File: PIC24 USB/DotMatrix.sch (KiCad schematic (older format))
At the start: 13 parts, among them Q2 MOSFET_N, Q3 MOSFET_N, Q4 MOSFET_N, Q5 MOSFET_N, Q6 MOSFET_N, Q7 MOSFET_N, Q8 MOSFET_N, U3 50mm_5x7_Dot_Matrix_Led_Displ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

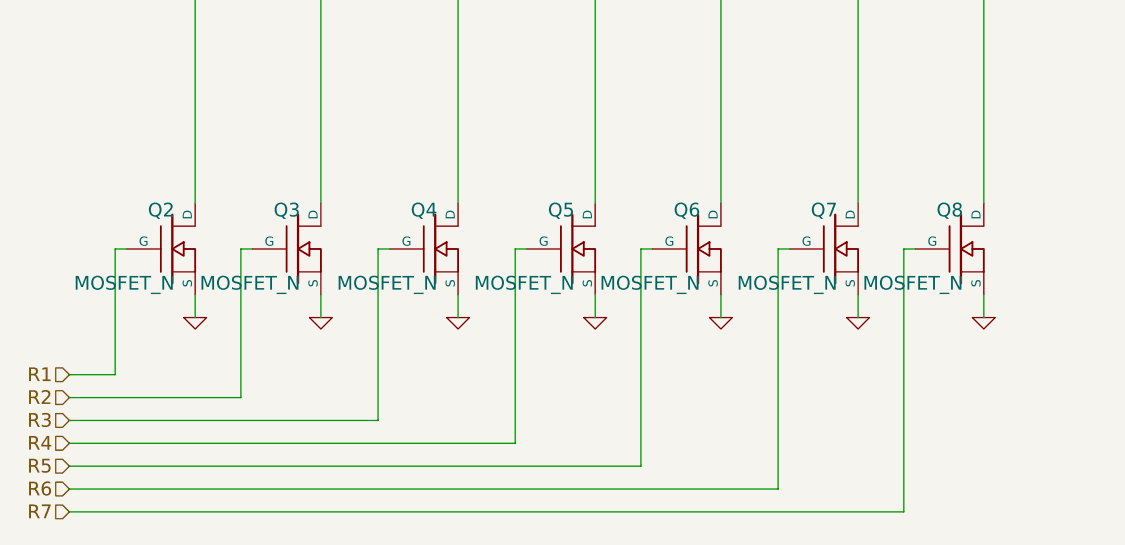
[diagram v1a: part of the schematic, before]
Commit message: shrinked, added temp sensor, updated gerbers and submitted them
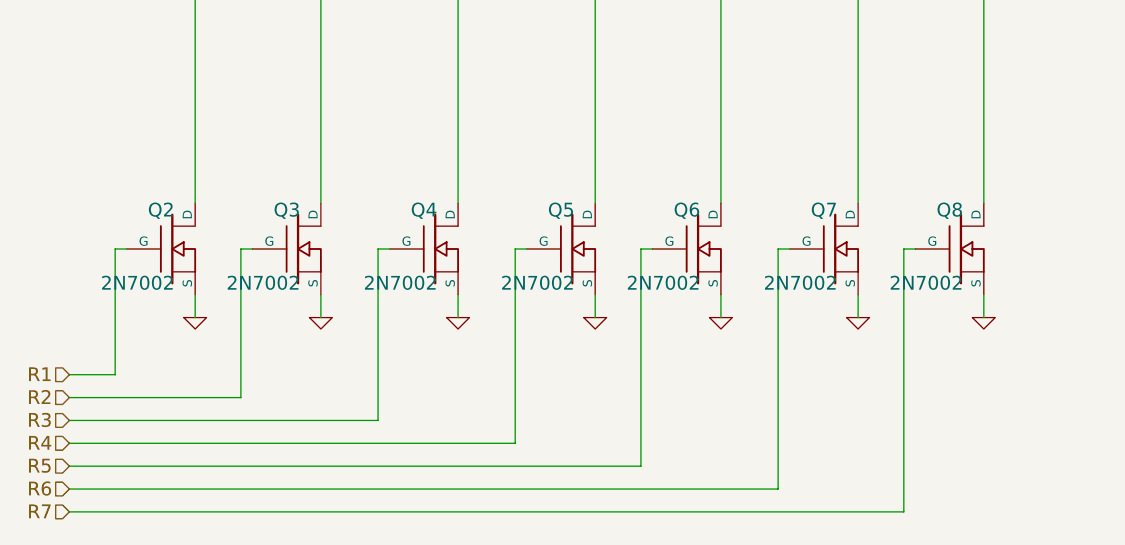
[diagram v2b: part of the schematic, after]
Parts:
- Q2, Q3, Q4, Q5, Q6, Q7, Q8: value MOSFET_N -> 2N7002
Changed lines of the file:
@@
 $Descr A4 11693 8268
 encoding utf-8
-Sheet 3 3
+Sheet 2 3
 Title ""
 Date ""
@@
 P 1200 4700
 F 0 "Q2" H 1210 4870 60  0000 R CNN
-F 1 "MOSFET_N" H 1210 4550 60  0000 R CNN
+F 1 "2N7002" H 1210 4550 60  0000 R CNN
 F 2 "SMD_Packages:SOT-23-GDS" H 1200 4700 60  0001 C CNN
 F 3 "" H 1200 4700 60  0000 C CNN
@@
 P 2350 4700
 F 0 "Q4" H 2360 4870 60  0000 R CNN
-F 1 "MOSFET_N" H 2360 4550 60  0000 R CNN
+F 1 "2N7002" H 2360 4550 60  0000 R CNN
 F 2 "SMD_Packages:SOT-23-GDS" H 2350 4700 60  0001 C CNN
 F 3 "" H 2350 4700 60  0000 C CNN
@@
 P 1750 4700
 F 0 "Q3" H 1760 4870 60  0000 R CNN
-F 1 "MOSFET_N" H 1760 4550 60  0000 R CNN
+F 1 "2N7002" H 1760 4550 60  0000 R CNN
 F 2 "SMD_Packages:SOT-23-GDS" H 1750 4700 60  0001 C CNN
 F 3 "" H 1750 4700 60  0000 C CNN
@@
 P 2950 4700
 F 0 "Q5" H 2960 4870 60  0000 R CNN
-F 1 "MOSFET_N" H 2960 4550 60  0000 R CNN
+F 1 "2N7002" H 2960 4550 60  0000 R CNN
 F 2 "SMD_Packages:SOT-23-GDS" H 2950 4700 60  0001 C CNN
 F 3 "" H 2950 4700 60  0000 C CNN
@@
 P 4100 4700
 F 0 "Q7" H 4110 4870 60  0000 R CNN
-F 1 "MOSFET_N" H 4110 4550 60  0000 R CNN
+F 1 "2N7002" H 4110 4550 60  0000 R CNN
 F 2 "SMD_Packages:SOT-23-GDS" H 4100 4700 60  0001 C CNN
 F 3 "" H 4100 4700 60  0000 C CNN
@@
 P 3500 4700
 F 0 "Q6" H 3510 4870 60  0000 R CNN
-F 1 "MOSFET_N" H 3510 4550 60  0000 R CNN
+F 1 "2N7002" H 3510 4550 60  0000 R CNN
 F 2 "SMD_Packages:SOT-23-GDS" H 3500 4700 60  0001 C CNN
 F 3 "" H 3500 4700 60  0000 C CNN
@@
 P 4650 4700
 F 0 "Q8" H 4660 4870 60  0000 R CNN
-F 1 "MOSFET_N" H 4660 4550 60  0000 R CNN
+F 1 "2N7002" H 4660 4550 60  0000 R CNN
 F 2 "SMD_Packages:SOT-23-GDS" H 4650 4700 60  0001 C CNN
 F 3 "" H 4650 4700 60  0000 C CNN
@@
 	1300 2900 1300 4500
 $Comp
-L GND #PWR35
+L GND #PWR37
 U 1 1 53E9FEF4
 P 1300 5000
-F 0 "#PWR35" H 1300 5000 30  0001 C CNN
+F 0 "#PWR37" H 1300 5000 30  0001 C CNN
 F 1 "GND" H 1300 4930 30  0001 C CNN
 F 2 "" H 1300 5000 60  0000 C CNN
@@
 $EndComp
 $Comp
-L GND #PWR36
+L GND #PWR38
 U 1 1 53E9FF16
 P 1850 5000
-F 0 "#PWR36" H 1850 5000 30  0001 C CNN
+F 0 "#PWR38" H 1850 5000 30  0001 C CNN
 F 1 "GND" H 1850 4930 30  0001 C CNN
 F 2 "" H 1850 5000 60  0000 C CNN
@@
 $EndComp
 $Comp
-L GND #PWR37
+L GND #PWR39
 U 1 1 53E9FF29
 P 2450 5000
-F 0 "#PWR37" H 2450 5000 30  0001 C CNN
+F 0 "#PWR39" H 2450 5000 30  0001 C CNN
 F 1 "GND" H 2450 4930 30  0001 C CNN
 F 2 "" H 2450 5000 60  0000 C CNN
@@
 $EndComp
 $Comp
-L GND #PWR38
+L GND #PWR40
 U 1 1 53E9FF3C
 P 3050 5000
-F 0 "#PWR38" H 3050 5000 30  0001 C CNN
+F 0 "#PWR40" H 3050 5000 30  0001 C CNN
 F 1 "GND" H 3050 4930 30  0001 C CNN
 F 2 "" H 3050 5000 60  0000 C CNN
@@
 $EndComp
 $Comp
-L GND #PWR39
+L GND #PWR41
 U 1 1 53EA0257
 P 3600 5000
-F 0 "#PWR39" H 3600 5000 30  0001 C CNN
+F 0 "#PWR41" H 3600 5000 30  0001 C CNN
 F 1 "GND" H 3600 4930 30  0001 C CNN
 F 2 "" H 3600 5000 60  0000 C CNN
@@
 $EndComp
 $Comp
-L GND #PWR40
+L GND #PWR42
 U 1 1 53EA025D
 P 4200 5000
-F 0 "#PWR40" H 4200 5000 30  0001 C CNN
+F 0 "#PWR42" H 4200 5000 30  0001 C CNN
 F 1 "GND" H 4200 4930 30  0001 C CNN
 F 2 "" H 4200 5000 60  0000 C CNN
@@
 $EndComp
 $Comp
-L GND #PWR41
+L GND #PWR43
 U 1 1 53EA0263
 P 4750 5000
-F 0 "#PWR41" H 4750 5000 30  0001 C CNN
+F 0 "#PWR43" H 4750 5000 30  0001 C CNN
 F 1 "GND" H 4750 4930 30  0001 C CNN
 F 2 "" H 4750 5000 60  0000 C CNN

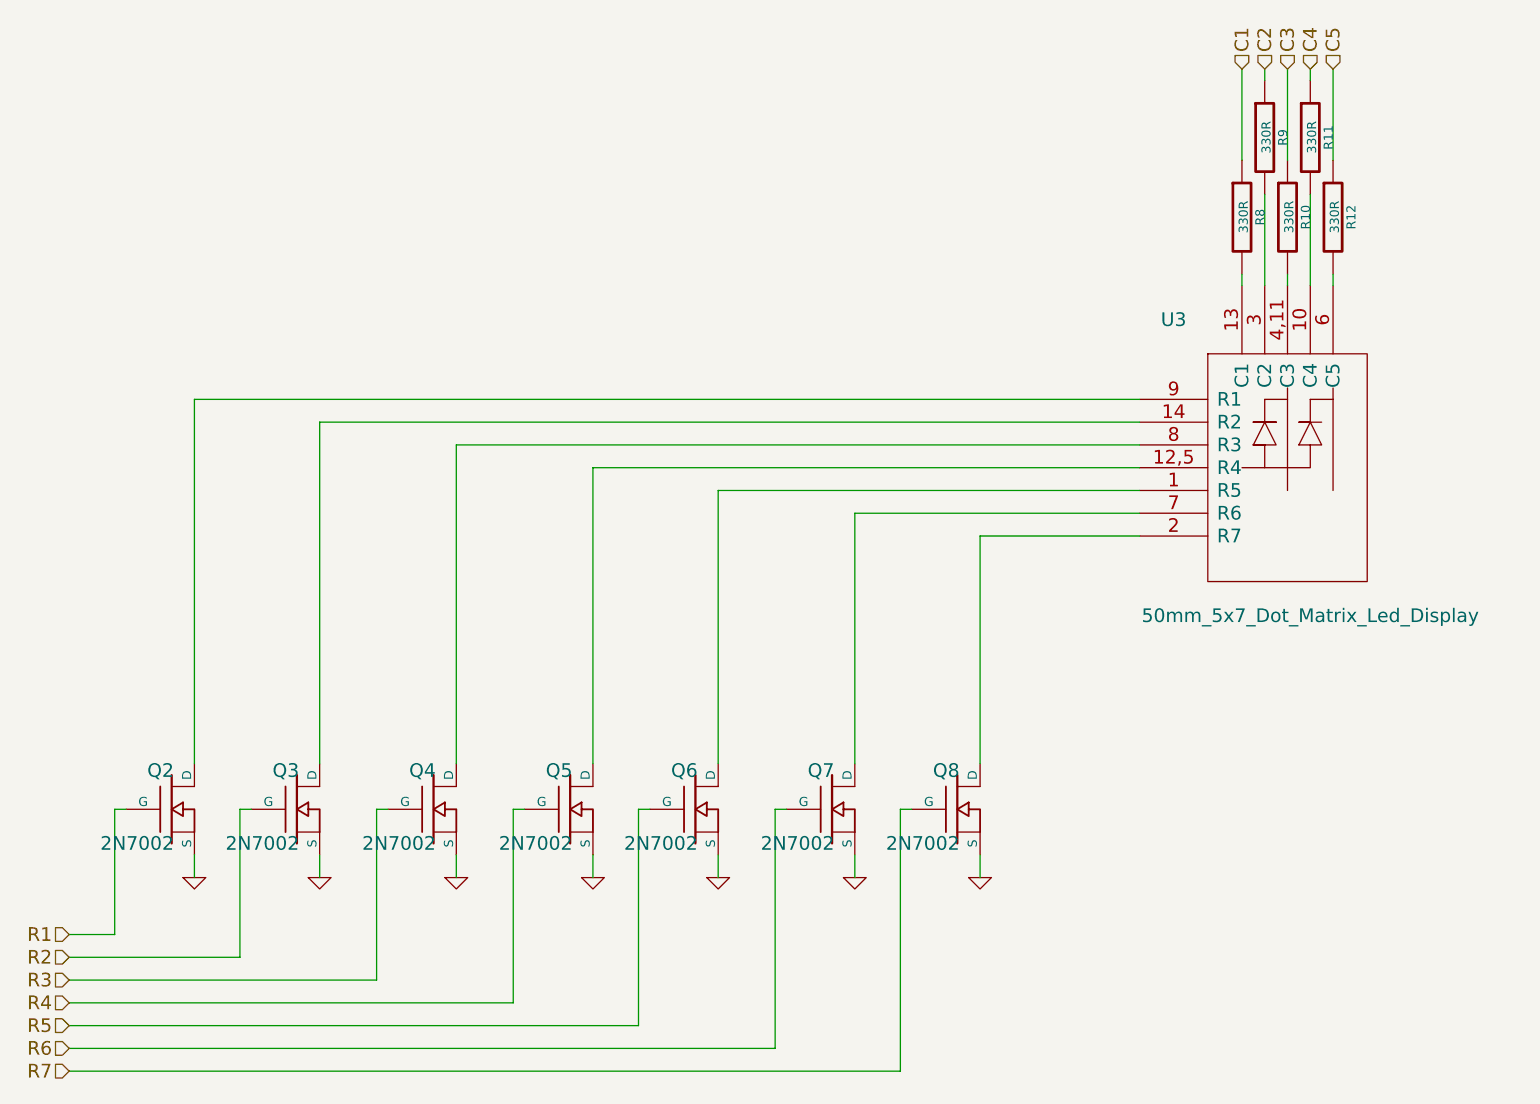
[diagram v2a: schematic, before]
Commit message: changed wrong polarity of led matrix in schematic, started correcting the layout
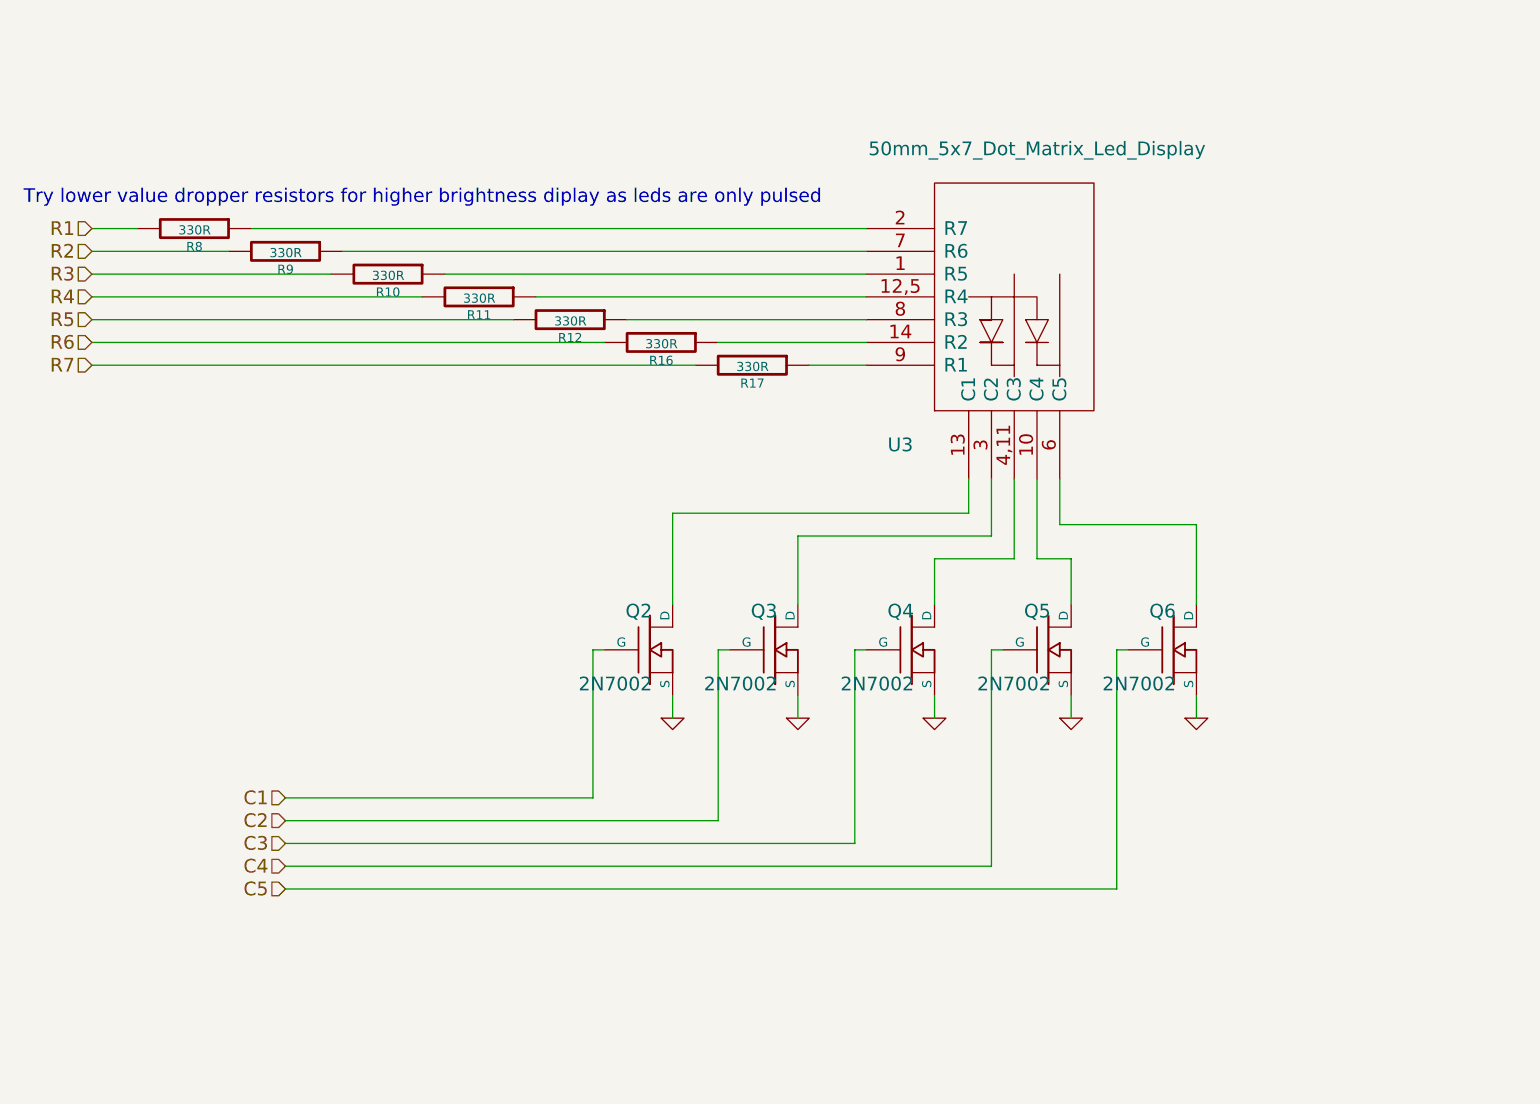
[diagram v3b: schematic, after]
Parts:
- removed Q7, Q8: 2N7002, SMD_Packages:SOT-23-GDS, symbol MOSFET_N
- added R16, R17: 330R, SMD_Packages:SMD-0603_r, symbol R
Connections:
- net C1: now also Q2.G; no longer R8.1
- net C2: now also Q3.G; no longer R9.1
- net C3: now also Q4.G; no longer R10.1
- net C4: now also Q5.G; no longer R11.1
- net C5: now also Q6.G; no longer R12.1
- net R1: now also R8.2; no longer Q2.G
- net R2: now also R9.2; no longer Q3.G
- net R3: now also R10.2; no longer Q4.G
- net R4: now also R11.2; no longer Q5.G
- net R5: now also R12.2; no longer Q6.G
- net R6: now also R16.2
- net R7: now also R17.2
- net at U3.1 (R5): now also R10.1; no longer Q6.D
- net at U3.10 (C4): now also Q5.D; no longer R11.2
- net at U3.12,5 (R4): now also R11.1; no longer Q5.D
- net at U3.13 (C1): now also Q2.D; no longer R8.2
- net at U3.14 (R2): now also R16.1; no longer Q3.D
- net at U3.2 (R7): now also R8.1
- net at U3.3 (C2): now also Q3.D; no longer R9.2
- net at U3.4,11 (C3): now also Q4.D; no longer R10.2
- net at U3.6 (C5): now also Q6.D; no longer R12.2
- net at U3.7 (R6): now also R9.1
- net at U3.8 (R3): now also R12.1; no longer Q4.D
- net at U3.9 (R1): now also R17.1; no longer Q2.D
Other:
- note added: "Try lower value dropper resistors for higher brightness diplay as leds are only pulsed"
- moved on the sheet: Q2, Q3, Q4, Q5, Q6, R10, R11, R12, R8, R9, U3

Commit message: Updated
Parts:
- R10, R11, R12, R16, R17, R8, R9: symbol R -> R-RESCUE-PIC24_USB_IR_Transmitter
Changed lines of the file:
@@
 EESchema Schematic File Version 2
+LIBS:PIC24_USB_IR_Transmitter-rescue
 LIBS:power
 LIBS:device
@@
 LIBS:led_hele
 LIBS:PIC24_USB_IR_Transmitter-cache
-EELAYER 24 0
+EELAYER 25 0
 EELAYER END
 $Descr A4 11693 8268
@@
 $EndComp
 $Comp
-L GND #PWR043
+L GND-RESCUE-PIC24_USB_IR_Transmitter #PWR043
 U 1 1 53E9FEF4
 P 3400 4300
@@
 $EndComp
 $Comp
-L GND #PWR044
+L GND-RESCUE-PIC24_USB_IR_Transmitter #PWR044
 U 1 1 53E9FF16
 P 3950 4300
@@
 $EndComp
 $Comp
-L GND #PWR045
+L GND-RESCUE-PIC24_USB_IR_Transmitter #PWR045
 U 1 1 53E9FF29
 P 4550 4300
@@
 $EndComp
 $Comp
-L GND #PWR046
+L GND-RESCUE-PIC24_USB_IR_Transmitter #PWR046
 U 1 1 53E9FF3C
 P 5150 4300
@@
 $EndComp
 $Comp
-L GND #PWR047
+L GND-RESCUE-PIC24_USB_IR_Transmitter #PWR047
 U 1 1 53EA0257
 P 5700 4300
@@
 	3400 4200 3400 4300
 $Comp
-L R R8
+L R-RESCUE-PIC24_USB_IR_Transmitter R8
 U 1 1 53EA066A
 P 1300 2150
@@
 $EndComp
 $Comp
-L R R9
+L R-RESCUE-PIC24_USB_IR_Transmitter R9
 U 1 1 53EA06A6
 P 1700 2250
@@
 $EndComp
 $Comp
-L R R10
+L R-RESCUE-PIC24_USB_IR_Transmitter R10
 U 1 1 53EA0720
 P 2150 2350
@@
 $EndComp
 $Comp
-L R R11
+L R-RESCUE-PIC24_USB_IR_Transmitter R11
 U 1 1 53EA0726
 P 2550 2450
@@
 $EndComp
 $Comp
-L R R12
+L R-RESCUE-PIC24_USB_IR_Transmitter R12
 U 1 1 53EA0746
 P 2950 2550
@@
 C5
 $Comp
-L R R16
+L R-RESCUE-PIC24_USB_IR_Transmitter R16
 U 1 1 545ADDA7
 P 3350 2650
@@
 $EndComp
 $Comp
-L R R17
+L R-RESCUE-PIC24_USB_IR_Transmitter R17
 U 1 1 545ADDE0
 P 3750 2750
